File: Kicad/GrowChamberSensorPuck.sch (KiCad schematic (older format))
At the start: 2 parts

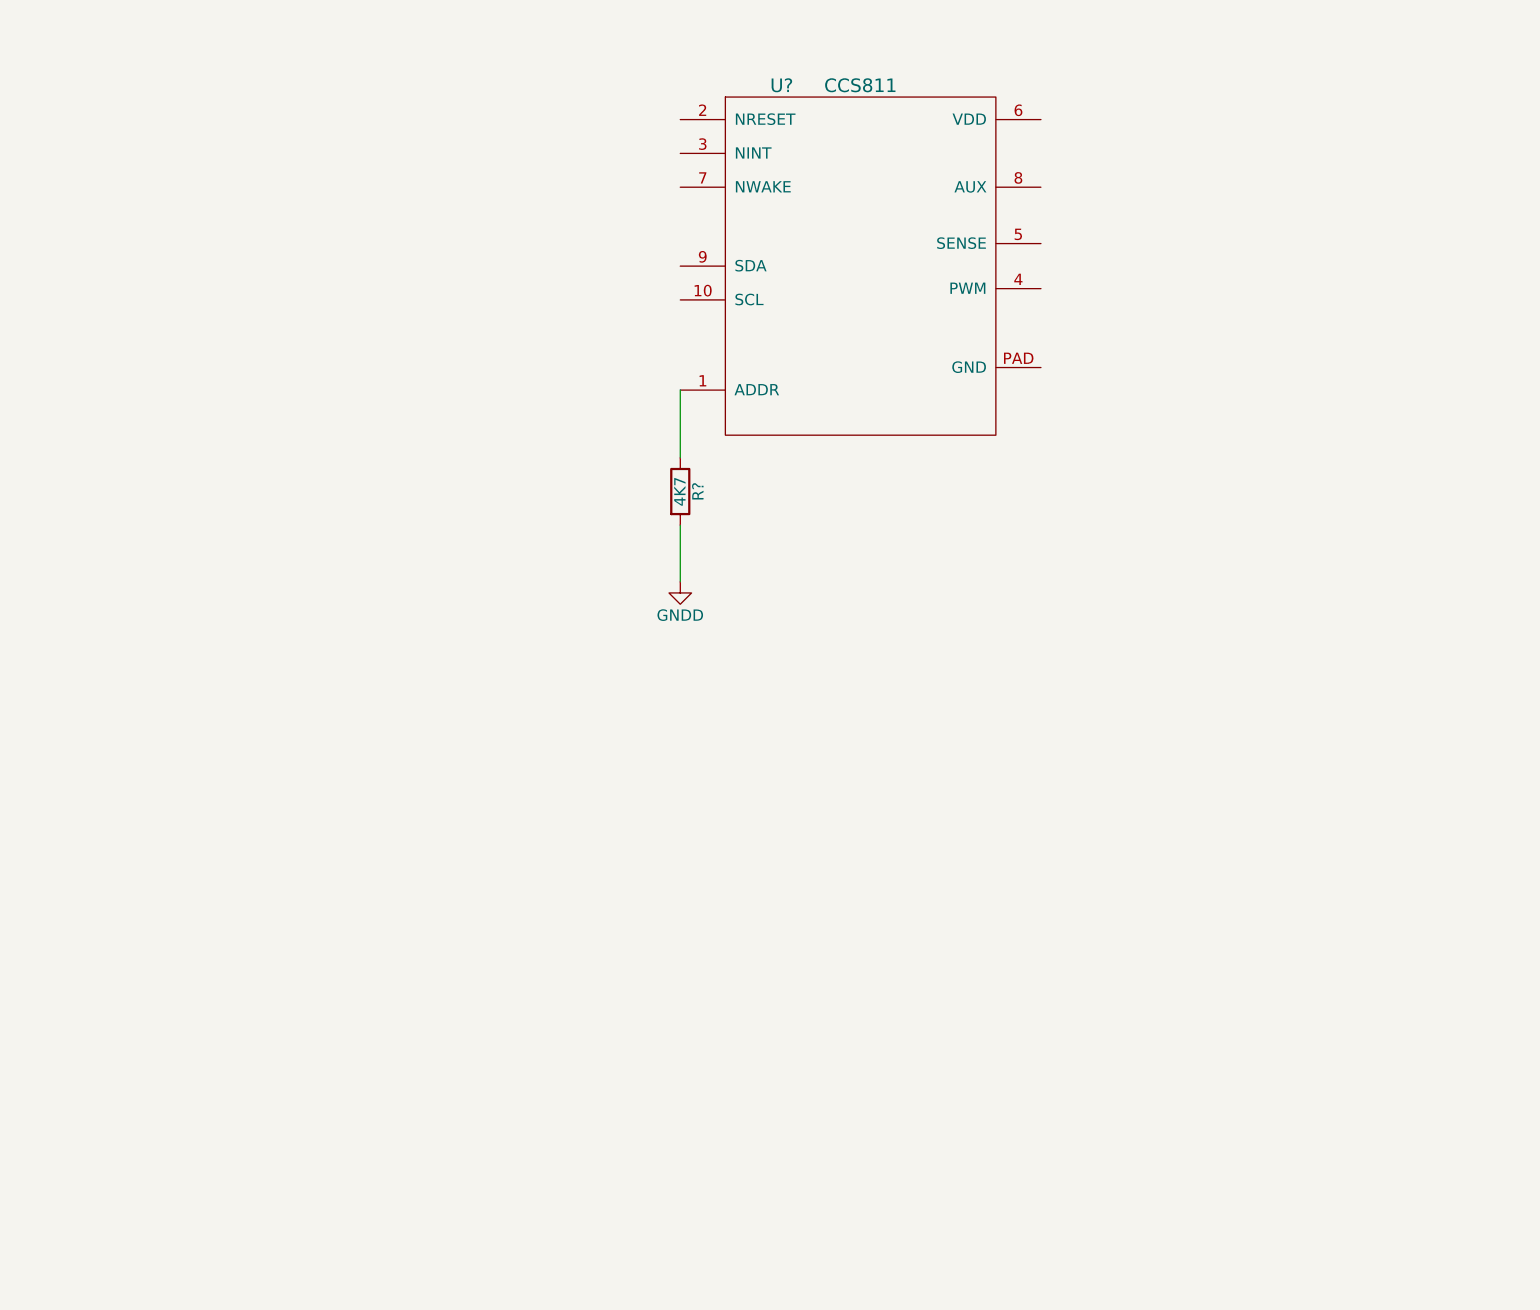
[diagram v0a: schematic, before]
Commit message: added Kicad eeSchema for sensor puck
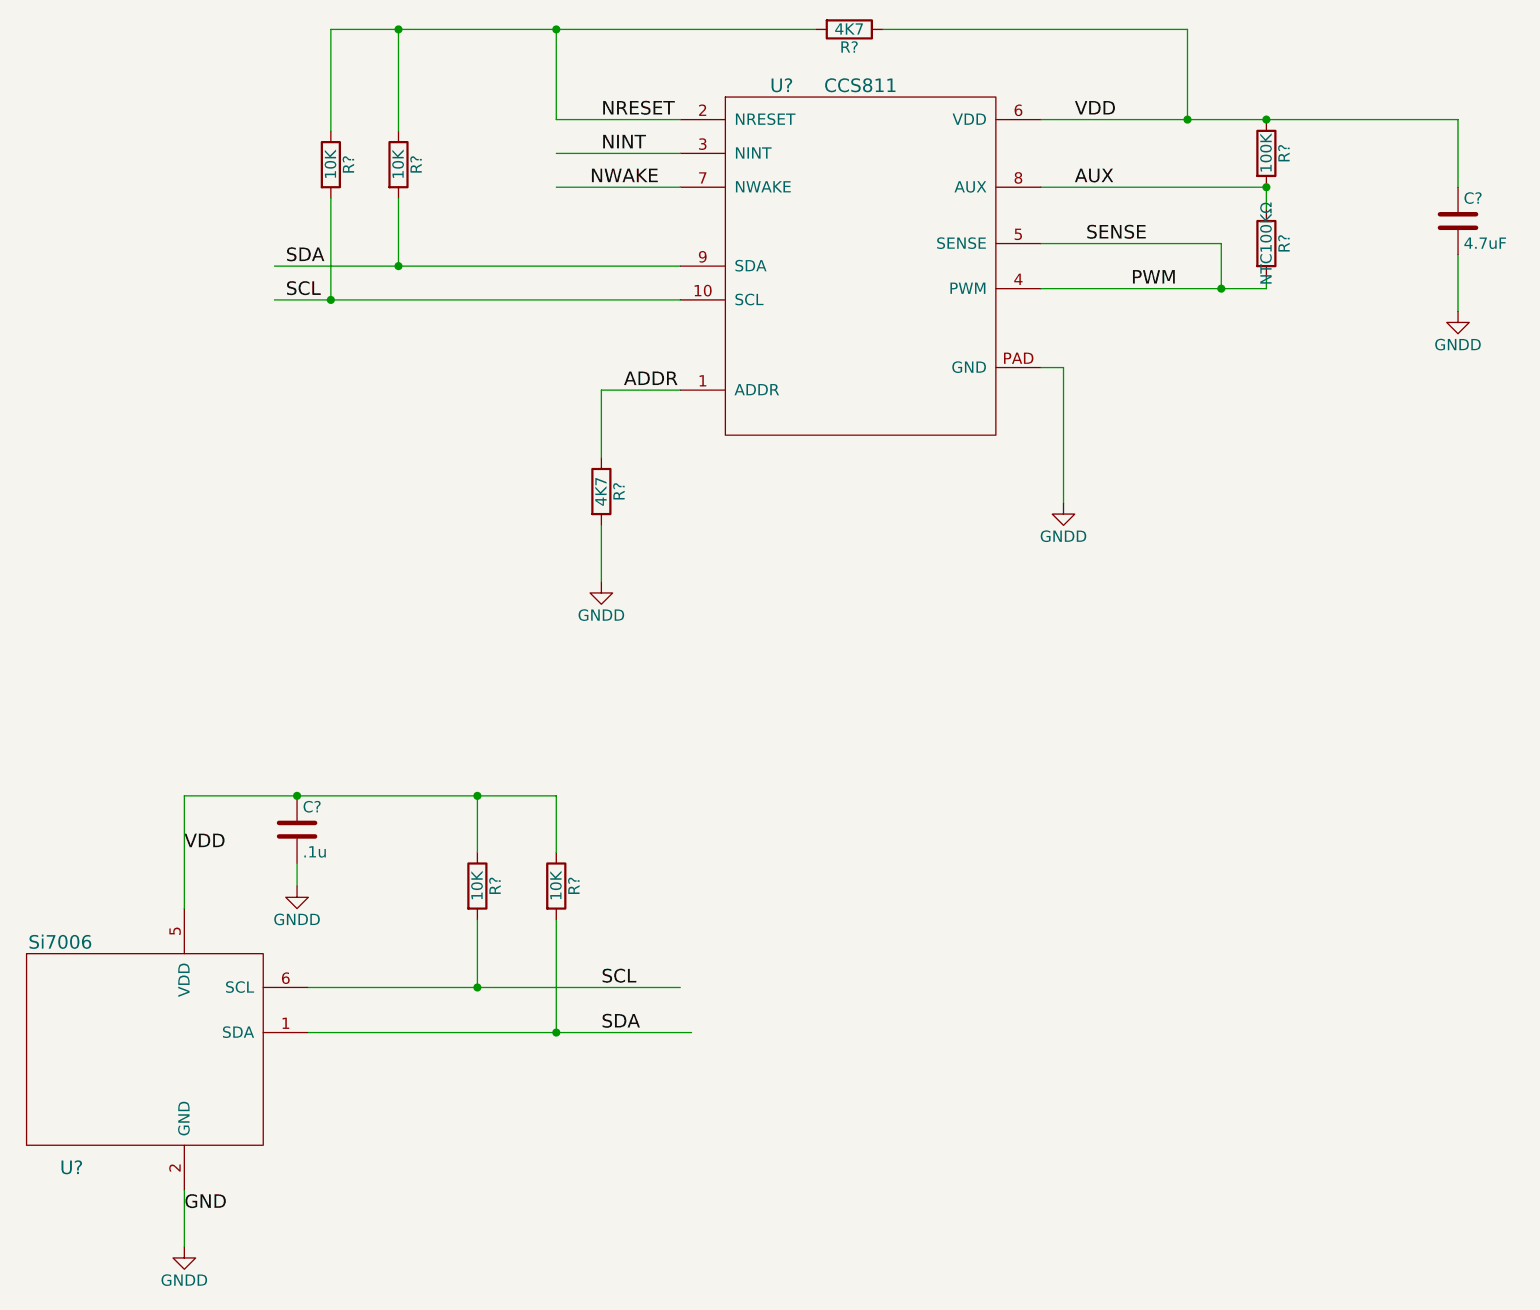
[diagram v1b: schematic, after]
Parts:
- added C?: 4.7uF, symbol C
- added C?: .1u, symbol C
- added R?: NTC100KΩ, symbol R
- added R?: 100K, symbol R
- added R?: 4K7, symbol R
- added R? (x4): 10K, symbol R
- added U?: Si7006, symbol Si7006
- R?: PN (none) -> R
- U?: PN (none) -> CCS811CT-ND
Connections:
- net labels added: ADDR, AUX, GND, NINT, NRESET, NWAKE, PWM, SCL, SDA, SENSE, VDD
- wire segments 2 -> 37
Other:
- moved on the sheet: R?
